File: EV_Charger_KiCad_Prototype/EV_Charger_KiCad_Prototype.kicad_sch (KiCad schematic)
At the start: 0 parts

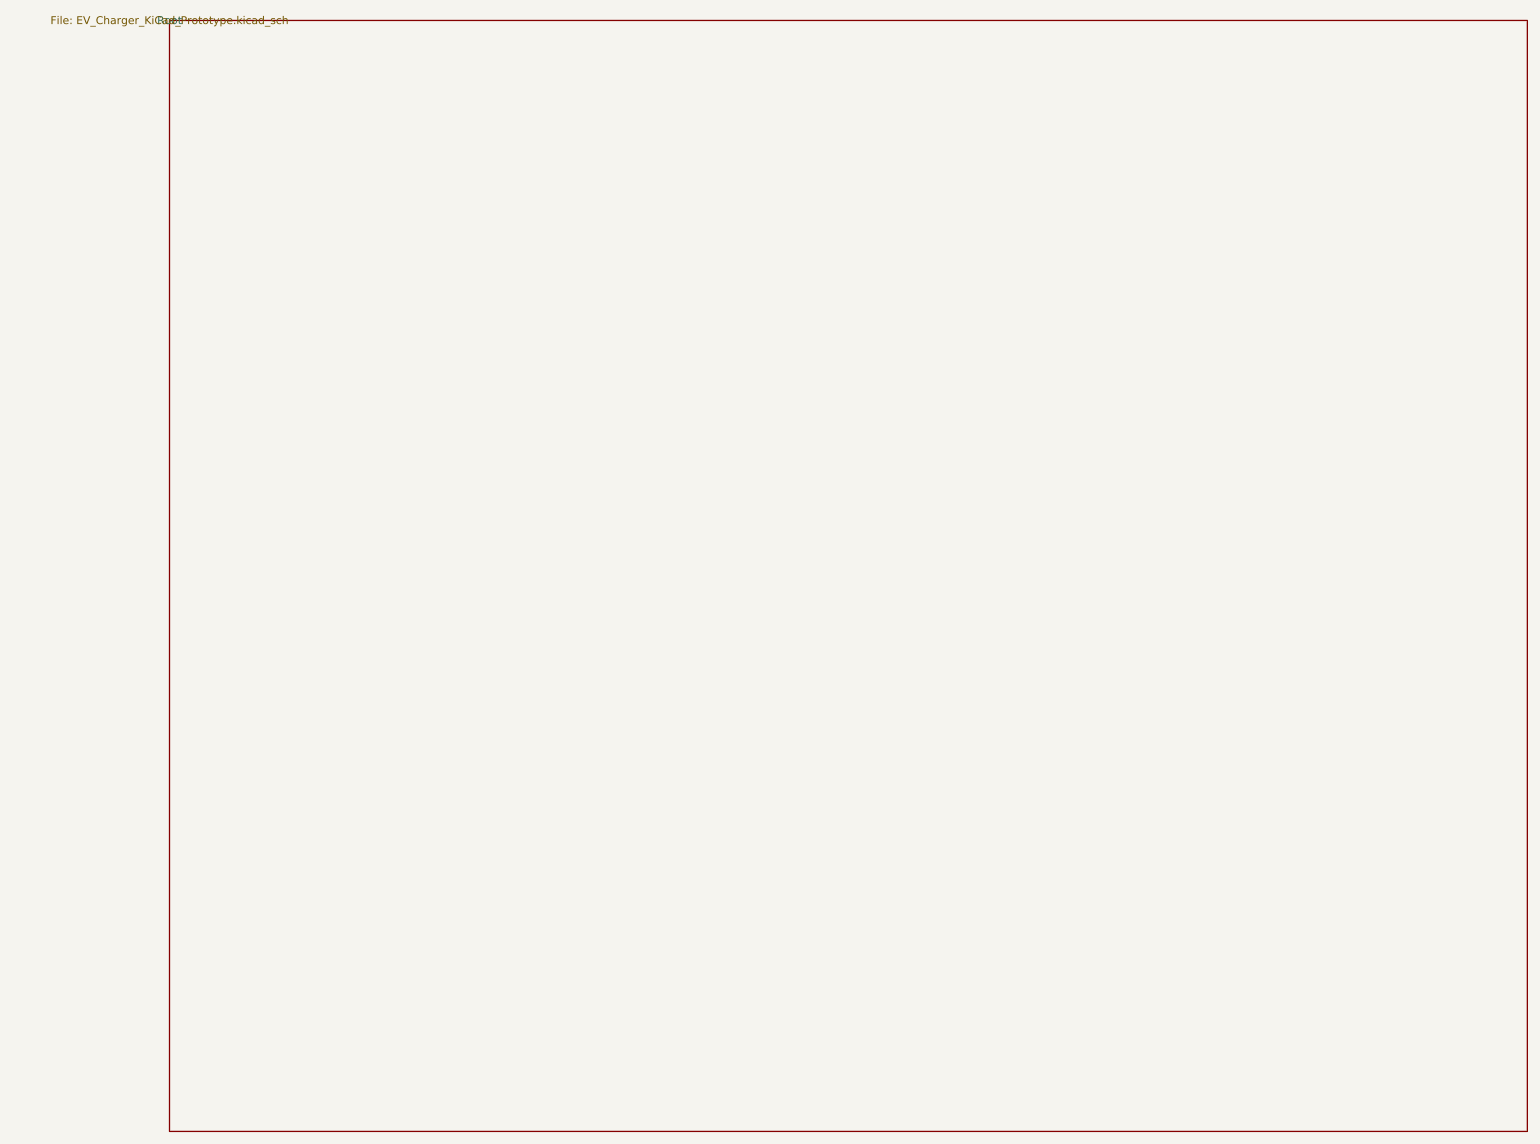
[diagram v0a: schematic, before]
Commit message: Adjust KiCad files for better KiCanvas compatibility
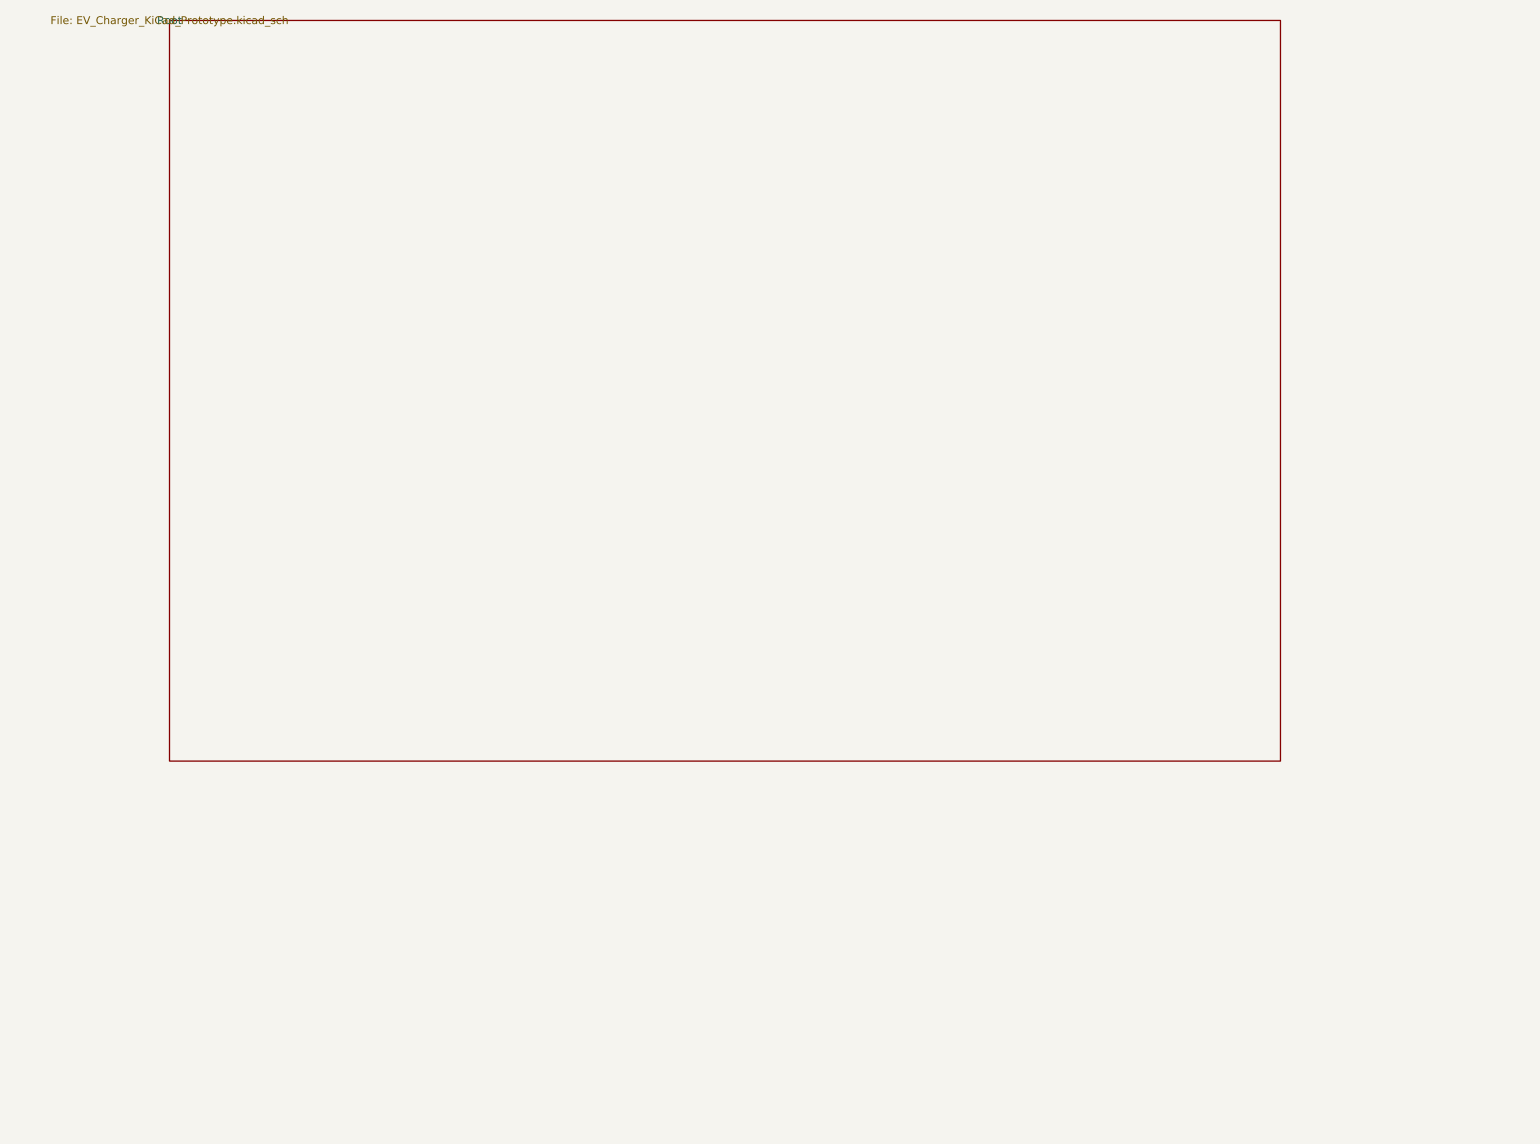
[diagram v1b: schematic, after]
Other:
- company: (none) -> AI Hardware Lab
- title: (none) -> EV Charger Controller Prototype
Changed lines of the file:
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@@
 (kicad_sch
-  (version 20250114)
+  (version 20240607)
   (generator "eeschema")
-  (generator_version "10.0")
+  (generator_version "8.99")
   (paper "A4")
+  (title_block
+    (title "EV Charger Controller Prototype")
+    (date "2026-08-01")
+    (rev "0.1")
+    (company "AI Hardware Lab")
+  )
   (sheet
     (at 0 0)
-    (size 220 180)
+    (size 180 120)
     (stroke (width 0.1) (type solid))
     (fill (color 0 0 0 0.0000))
     (property "Sheetname" "Root")
     (property "Sheetfile" "EV_Charger_KiCad_Prototype.kicad_sch")
-    (text "EV Charger Controller" (at 20 24 0))
-    (text "Main Control MCU" (at 20 58 0))
-    (text "Safety Supervisor" (at 20 82 0))
-    (text "Power / Protection" (at 20 106 0))
-    (text "Measurement Front-End" (at 20 130 0))
-    (text "Communication Stack" (at 20 154 0))
+    (text "EV Charger Controller" (at 12 20 0))
+    (text "Main Control MCU" (at 12 42 0))
+    (text "Safety Supervisor" (at 12 60 0))
+    (text "Power / Protection" (at 12 78 0))
+    (text "Measurement Front-End" (at 12 96 0))
+    (text "Communication Stack" (at 12 114 0))
   )
   (sheet_instances
